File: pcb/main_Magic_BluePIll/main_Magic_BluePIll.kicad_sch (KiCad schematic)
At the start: 46 parts, among them J1 PW, J10 ESC1, J11 ESC2, J12 ESC3, J2 MPU6050, J3 ST_Link, J4 LiPo, J9 Sensors, Q1 IRLML2502, SW1 Power_SW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

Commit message: stm32 pcb schematic update
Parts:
- removed C24, C6: 100nF, Capacitor_SMD:C_0805_2012Metric, symbol Device:C_Small
- removed D2, D3: WS2812B, LED_SMD:LED_WS2812B_PLCC4_5.0x5.0mm_P3.2mm, symbol LED:WS2812B
- removed J10: ESC1, Connector_JST:JST_XH_S2B-XH-A_1x02_P2.50mm_Horizontal, symbol Connector:Conn_01x02_Pin
- removed J11: ESC2, Connector_JST:JST_XH_S2B-XH-A_1x02_P2.50mm_Horizontal, symbol Connector:Conn_01x02_Pin
- removed J12: ESC3, Connector_JST:JST_XH_S2B-XH-A_1x02_P2.50mm_Horizontal, symbol Connector:Conn_01x02_Pin
- removed JP1: ESP_JP, Resistor_SMD:R_1206_3216Metric, symbol Jumper:Jumper_2_Small_Open
- removed JP2: LED_JP, Resistor_SMD:R_1206_3216Metric, symbol Jumper:Jumper_2_Small_Open
- removed R1: 330, Resistor_SMD:R_0805_2012Metric, symbol Device:R_Small
- added D2: LED_RGB, LED_SMD:LED_RGB_5050-6, symbol Device:LED_RGB
- added D5: LED_ON, MixLib:LED_0805_2012Metric, symbol Device:LED_Small
- added J5: ESC, Connector_JST:JST_XH_B6B-XH-A_1x06_P2.50mm_Vertical, symbol Connector:Conn_01x06_Pin
- added R10, R11, R12: 470, Resistor_SMD:R_0805_2012Metric, symbol Device:R_Small
- added R13: 1k, Resistor_SMD:R_0603_1608Metric, symbol Device:R_Small
- added R3: 330k, Resistor_SMD:R_1206_3216Metric, symbol Device:R_Small
- added R4: 100k, Resistor_SMD:R_1206_3216Metric, symbol Device:R_Small
- added U2: AMS1117CD-3.3, Package_TO_SOT_SMD:TO-252-3_TabPin2, symbol Regulator_Linear:AMS1117CD-3.3
- D4: value LED_ON -> LED_SW
- R5: value 330 -> 1k; footprint Resistor_SMD:R_0805_2012Metric -> Resistor_SMD:R_1206_3216Metric
- U6: value CN3903 -> CN3905
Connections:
- net VDD_ESP is gone; now on net +3.3V: C3.1, C4.1
- net +3.3V: now also U1.20 (3V3), U1.38 (3V3), D5.2 (A), U2.2 (VO); no longer D4.2 (A), R5.2, U6.3 (OUT)
- net GND: now also U1.19 (GND), U1.39 (GND), U1.40 (GND), D2.1 (RK), D2.2 (GK), D2.3 (BK), J5.6 (Pin_6), R13.2, R4.2, U2.1 (GND)
- net VM: now also J5.5 (Pin_5)
- net Vb: now also R3.1
- net V_bat: now reaches R5.1
- new net: D2.5 (GA), R11.1
- new net: R3.2, R4.1, R5.2
- new net: D5.1 (K), R13.1
- new net: D2.4 (BA), R10.1
- new net: D2.6 (RA), R12.1
- new net +5V: D4.2 (A), U2.3 (VI), U6.3 (OUT)
- new net Curr: J5.1 (Pin_1)
- new net ESC_M1: J5.4 (Pin_4)
- new net ESC_M2: J5.3 (Pin_3)
- new net ESC_M3: J5.2 (Pin_2)
- new net RGB_B: R10.2
- new net RGB_G: R11.2
- new net RGB_R: R12.2
- no-connect marks 2 -> 4
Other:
- note added: "(I/O)"
- note added: "5V pin"
- note added: "ADC"
- note added: "DAC"
- note added: "Digital"
- note added: "In:"
- note added: "Out:"
- note added: "PWM"
- note removed: "Programming"
- moved on the sheet: C2, C28, C3, C4, D1, D4, H1, H10, H11, H12, H2, H3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

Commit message: bluepill pcb
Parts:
- removed H5, H6: M3, MountingHole:MountingHole_3mm, symbol Mechanical:MountingHole
- added D3, D7: SS14, Diode_SMD:D_SMA, symbol Device:D_Schottky_Small
- added R1: 10k, Resistor_SMD:R_0805_2012Metric, symbol Device:R_Small
- added SW2: PUSH_2, MixLib:SW_Push_Sw-3424p_Handsolder, symbol Switch:SW_Push
- added U3: HC05, MixLib:HC05, symbol MixLib:HC05
- H11, H12: value M3 -> M2; footprint MountingHole:MountingHole_3mm -> MountingHole:MountingHole_2.2mm_M2
- J3: footprint Connector_PinHeader_2.54mm:PinHeader_1x05_P2.54mm_Horizontal -> Connector_PinHeader_2.54mm:PinHeader_1x05_P2.54mm_Vertical
- SW4: value BUTTON_Push -> PUSH_1
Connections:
- net +3.3V: now also U1.44 (3V3), SW2.1, U3.VCC
- net +5V: now also D3.1 (K), D7.1 (K); no longer U6.3 (OUT)
- net BUTTON: no longer R9.2, SW4.2
- net GND: now also J3.4 (Pin_4), U1.41 (GND), R1.1, U3.GND; no longer J4.2 (Pin_2)
- net VM: no longer J4.1 (Pin_1)
- net at J3.5 (Pin_5): now also D7.2 (A); no longer U1.41 (GND)
- net SWCLK: now reaches U1.42 (SWCLK)
- net SWCLK: now also J3.2 (Pin_2); no longer J3.4 (Pin_4)
- net SWIO: now reaches J3.3 (Pin_3), U1.43 (SWIO)
- new net: D3.2 (A), U6.3 (OUT)
- new net PUSH_1: R9.2, SW4.2
- new net PUSH_2: R1.2, SW2.2
- no-connect marks 4 -> 11
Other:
- note added: "Battery level"
- note added: "I2C Connections"
- note added: "Programming"
- note removed: "I2C Connectíons"
- moved on the sheet: C2, C28, C3, C4, D1, D2, D4, D5, D6, H1, H10, H2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

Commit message: components arranged in bluepill pcb
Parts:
- removed C2: 100uF, Capacitor_THT:CP_Radial_D8.0mm_P3.50mm, symbol Device:C_Polarized_Small
- removed C28: 470uF, Capacitor_THT:CP_Radial_D8.0mm_P3.50mm, symbol Device:C_Polarized_Small
- removed D7: SS14, Diode_SMD:D_SMA, symbol Device:D_Schottky_Small
- removed J1: PW, Connector_JST:JST_XH_B2B-XH-A_1x02_P2.50mm_Vertical, symbol Connector:Conn_01x02_Pin
- removed J3: ST_Link, Connector_PinHeader_2.54mm:PinHeader_1x05_P2.54mm_Vertical, symbol Connector:Conn_01x05_Pin
- removed J4: LiPo, Connector_JST:JST_XH_S2B-XH-A_1x02_P2.50mm_Horizontal, symbol Connector:Conn_01x02_Pin
- removed R2: 1k, Resistor_SMD:R_1206_3216Metric, symbol Device:R_Small
- added C1, C5: 100nF, Capacitor_SMD:C_0603_1608Metric, symbol Device:C_Small
- added C6, C7: 10uF, Capacitor_SMD:C_0805_2012Metric, symbol Device:C_Small
- C3: value 22uF -> 10UF
- D1, D3: footprint Diode_SMD:D_SMA -> Diode_SMD:D_SOD-123
- D4: value LED_SW -> LED_5V
- D5: value LED_ON -> LED_3V3
- R13: value 1k -> 4.7k
- R3, R4, R5: footprint Resistor_SMD:R_1206_3216Metric -> Resistor_SMD:R_0805_2012Metric
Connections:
- net +3.3V: now also C5.1, C7.1
- net +5V: now also C1.1, C6.1
- net GND: now also C1.2, C5.2, C6.2, C7.2
- net SCL: now also U1.16 (PB8)
- net SDA: now also U1.17 (PB9)
- net VM: now also R3.1
- net Vb: now also BZ1.1 (+); no longer R3.1
- net BL_RX: now reaches U1.6 (PA9)
- net BL_RX: now also U3.RXD
- net BL_TX: now reaches U1.7 (PA10)
- net BL_TX: now also U3.TXD
- no-connect marks 11 -> 6
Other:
- note removed: "Programming"
- moved on the sheet: BZ1, C3, C4, D1, D3, D4, D5, D6, H11, H12, Q1, R13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

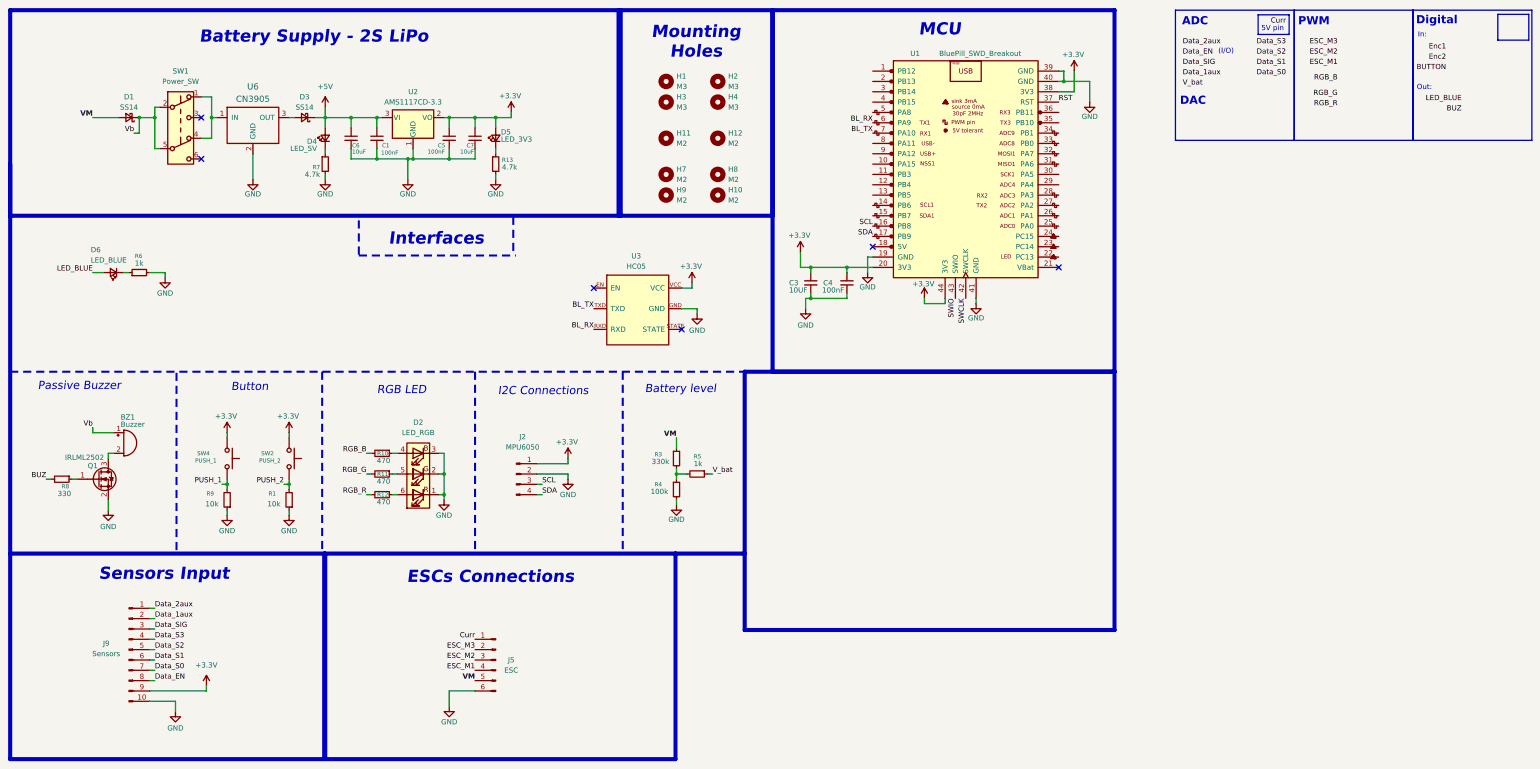
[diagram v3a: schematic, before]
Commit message: Routing of STM32F103 PCB done
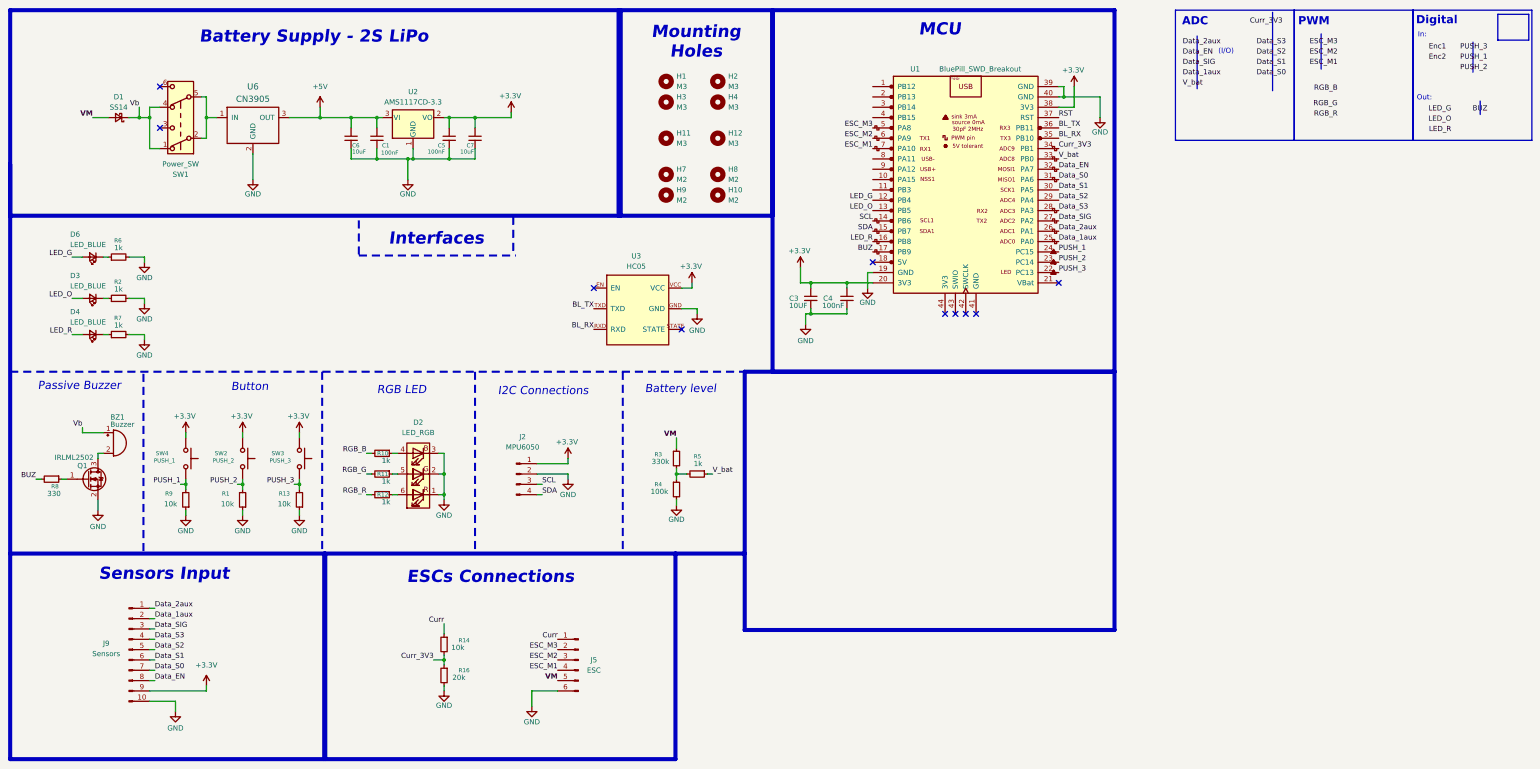
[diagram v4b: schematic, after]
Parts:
- removed D3: SS14, Diode_SMD:D_SOD-123, symbol Device:D_Schottky_Small
- removed D5: LED_3V3, MixLib:LED_0805_2012Metric, symbol Device:LED_Small
- added D3: LED_BLUE, MixLib:LED_0805_2012Metric, symbol Device:LED_Small
- added R14: 10k, Resistor_SMD:R_0805_2012Metric, symbol Device:R_Small
- added R16: 20k, Resistor_SMD:R_0805_2012Metric, symbol Device:R_Small
- added R2: 1k, Resistor_SMD:R_0603_1608Metric, symbol Device:R_Small
- added SW3: PUSH_3, MixLib:SW_Push_Sw-3424p_Handsolder, symbol Switch:SW_Push
- D4: value LED_5V -> LED_BLUE
- H11, H12: value M2 -> M3; footprint MountingHole:MountingHole_2.2mm_M2 -> MountingHole:MountingHole_3mm
- R1, R9: footprint Resistor_SMD:R_0805_2012Metric -> Resistor_SMD:R_0603_1608Metric
- R10, R11, R12: value 470 -> 1k; footprint Resistor_SMD:R_0805_2012Metric -> Resistor_SMD:R_0603_1608Metric
- R13: value 4.7k -> 10k
- R7: value 4.7k -> 1k
- SW1: footprint Button_Switch_SMD:SW_DPDT_CK_JS202011JCQN -> MixLib:SW_DPDT_SLIDE_THT
- U1: footprint MixLib:BluePill_SWD -> MixLib:BluePill
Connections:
- net LED_BLUE is gone; now on net LED_G: D6.2 (A)
- net +3.3V: now also SW3.1; no longer U1.44 (3V3)
- net +5V: now also U6.3 (OUT); no longer D4.2 (A)
- net BL_RX: now also U1.35 (PB10); no longer U1.6 (PA9)
- net BL_TX: now also U1.36 (PB11); no longer U1.7 (PA10)
- net BUZ: now also U1.17 (PB9)
- net Curr: now also R14.1
- net Data_1aux: now also U1.25 (PA0)
- net Data_2aux: now also U1.26 (PA1)
- net Data_EN: now also U1.32 (PA7)
- net Data_S0: now also U1.31 (PA6)
- net Data_S1: now also U1.30 (PA5)
- net Data_S2: now also U1.29 (PA4)
- net Data_S3: now also U1.28 (PA3)
- net Data_SIG: now also U1.27 (PA2)
- net ESC_M1: now also U1.7 (PA10)
- net ESC_M2: now also U1.6 (PA9)
- net ESC_M3: now also U1.5 (PA8)
- net GND: now also R13.1, R16.2, R2.2; no longer R13.2, U1.41 (GND)
- net PUSH_1: now also U1.24 (PC15)
- net PUSH_2: now also U1.23 (PC14)
- net SCL: now also U1.14 (PB6); no longer U1.16 (PB8)
- net SDA: now also U1.15 (PB7); no longer U1.17 (PB9)
- net V_bat: now also U1.33 (PB0)
- net Vb: now also SW1.1 (A), SW1.4 (A); no longer SW1.2 (B), SW1.5 (B)
- net LED_G: now reaches U1.12 (PB4)
- net LED_O: now reaches U1.13 (PB5)
- net LED_O: now also D3.2 (A)
- net PUSH_3: now reaches U1.22 (PC13)
- net PUSH_3: now also R13.2, SW3.2
- net Curr_3V3: now reaches U1.34 (PB1)
- net Curr_3V3: now also R14.2, R16.1
- net SWCLK: no longer names the net of U1.42 (SWCLK)
- net SWIO: no longer names the net of U1.43 (SWIO)
- new net: D3.1 (K), R2.1
- new net: SW1.2 (B), SW1.5 (B), U6.1 (IN)
- new net LED_R: D4.2 (A), U1.16 (PB8)
- no-connect marks 6 -> 10
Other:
- note removed: "5V pin"
- note removed: "DAC"
- moved on the sheet: BZ1, C3, C4, D1, D6, J5, Q1, R1, R6, R8, R9, SW1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

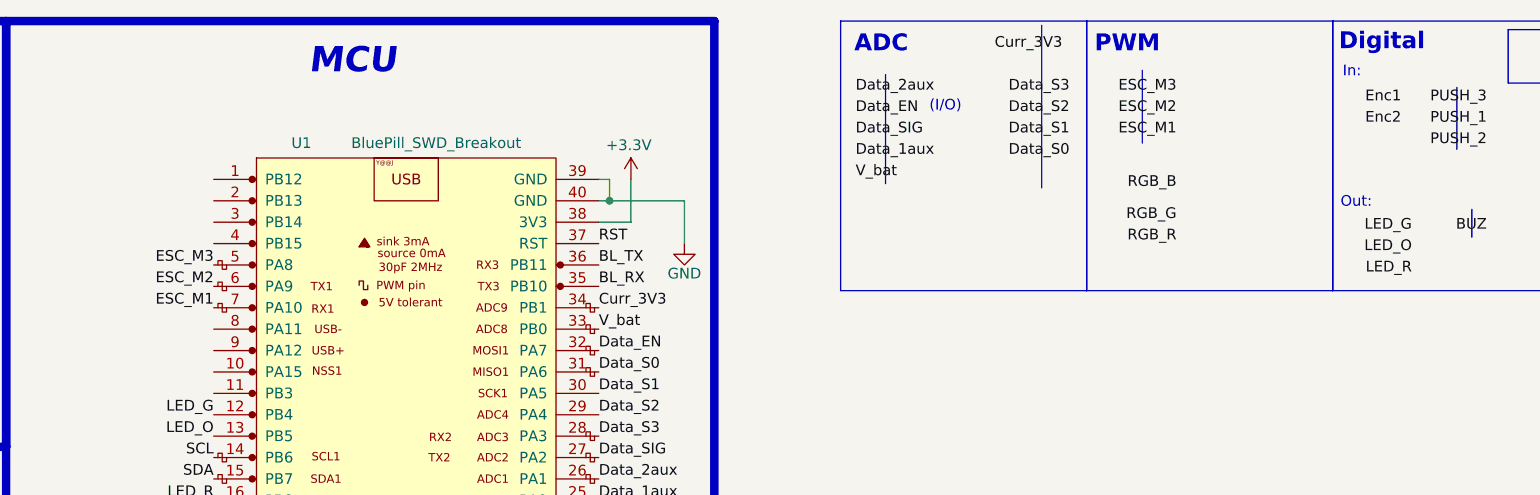
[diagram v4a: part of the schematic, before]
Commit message: RGB led added to STM32 pcb
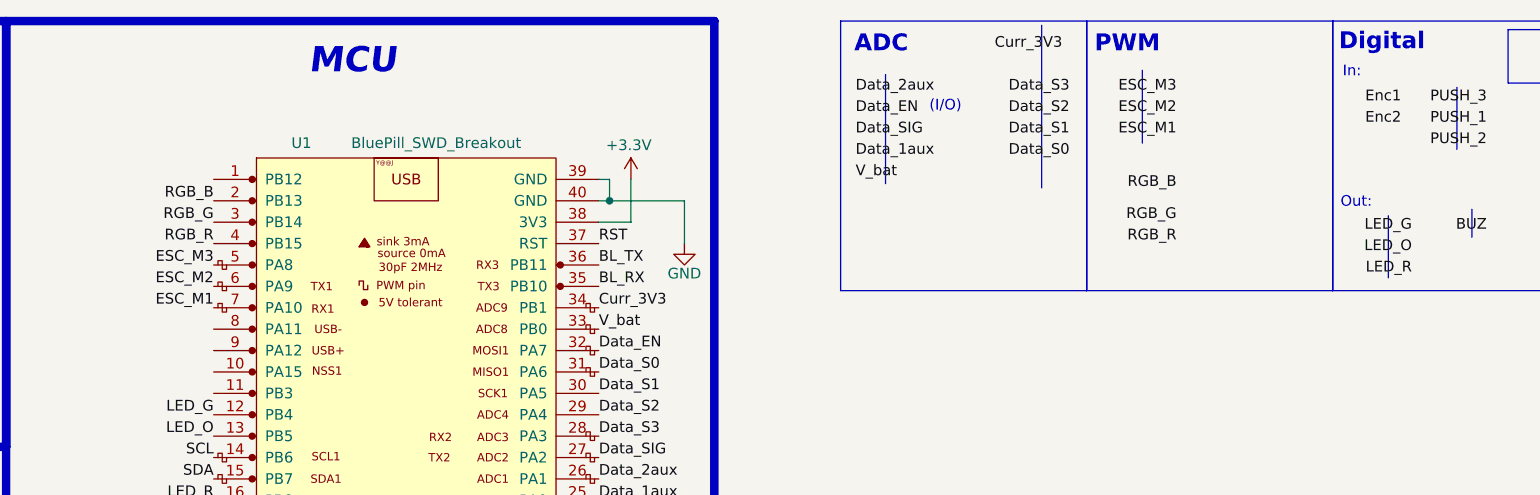
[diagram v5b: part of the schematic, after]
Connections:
- net RGB_B: now also U1.2 (PB13)
- net RGB_G: now also U1.3 (PB14)
- net RGB_R: now also U1.4 (PB15)
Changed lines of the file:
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@@
 		)
 	)
+	(polyline
+		(pts
+			(xy 364.236 36.068) (xy 364.236 43.434)
+		)
+		(stroke
+			(width 0)
+			(type default)
+		)
+	)
 	(wire
 		(pts
@@
 		)
 	)
+	(label "RGB_B"
+		(at 224.79 34.29 180)
+		(effects
+			(font
+				(size 1.27 1.27)
+			)
+			(justify right bottom)
+		)
+	)
 	(label "BUZ"
 		(at 19.05 128.27 180)
@@
 		)
 	)
+	(label "RGB_R"
+		(at 224.79 39.37 180)
+		(effects
+			(font
+				(size 1.27 1.27)
+			)
+			(justify right bottom)
+		)
+	)
 	(label "Data_S1"
 		(at 326.39 26.67 180)
@@
 		)
 	)
+	(label "RGB_G"
+		(at 224.79 36.83 180)
+		(effects
+			(font
+				(size 1.27 1.27)
+			)
+			(justify right bottom)
+		)
+	)

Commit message: minor changes
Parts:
- added D5: LED_BLUE, MixLib:LED_0805_2012Metric, symbol Device:LED_Small
- added R15: 10k, Resistor_SMD:R_0603_1608Metric, symbol Device:R_Small
- added R17: 1k, Resistor_SMD:R_0603_1608Metric, symbol Device:R_Small
- added SW5: PUSH_1, MixLib:SW_Push_Sw-3424p_Handsolder, symbol Switch:SW_Push
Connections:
- net +3.3V: now also D5.2 (A), SW5.1
- net GND: now also R15.1
- new net: D5.1 (K), R17.2
- new net PC13: R15.2, R17.1, SW5.2
